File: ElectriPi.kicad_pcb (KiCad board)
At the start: 2 copper layers, 65 x 56 mm, 45 parts, among them J1 2444, J2 JST XH 01x02, J3 JST XH 01x02, J6 Raspberry_Pi_2_3, J8 JST XH 01x02, Q1 30V 4A 44mΩ, Q2 50nA 150V 200mW 200mA, Q3 30V 4A 44mΩ, U1 XL4015

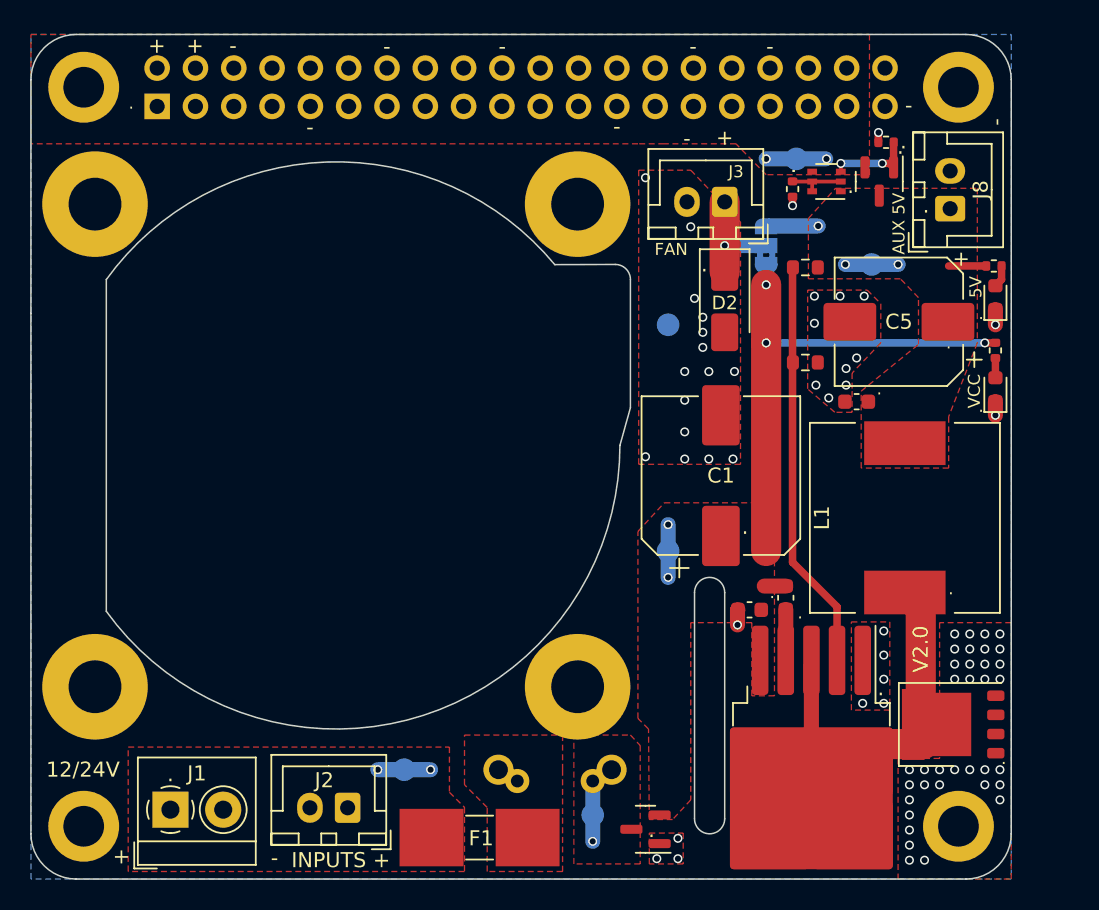
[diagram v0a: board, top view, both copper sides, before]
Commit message: First pass of layout complete
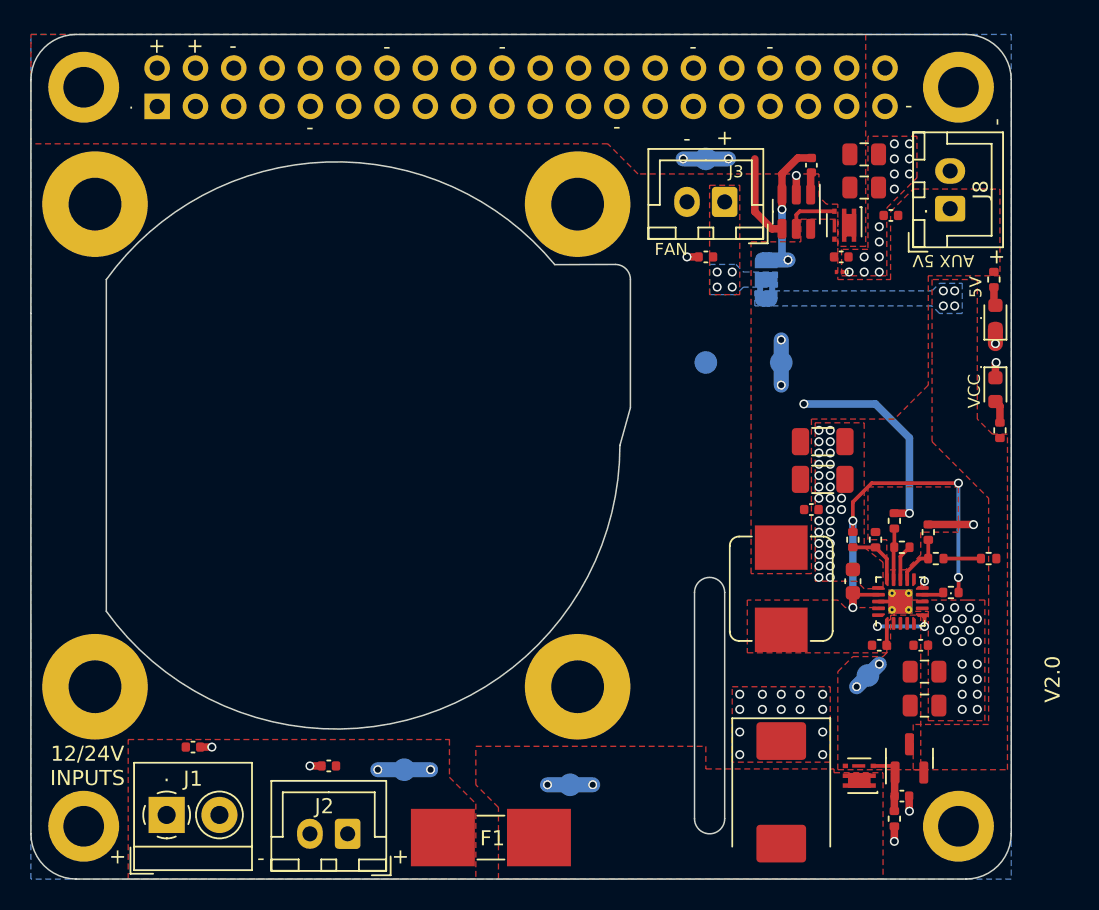
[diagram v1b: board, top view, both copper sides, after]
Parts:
- removed D2: SS54, Diode_SMD:D_SMA
- removed the G*** at (135.1, 81.0)
- removed Q3: 30V 4A 44mΩ, Package_TO_SOT_SMD:SOT-23
- removed R10: 10K, Resistor_SMD:R_0603_1608Metric
- removed R2: 47K, Resistor_SMD:R_0402_1005Metric
- removed R9: 3.3K, Resistor_SMD:R_0603_1608Metric
- removed TH1: ICL, Inrush_Limiter:5_OR_7pt5_PITCH_ICL
- added C10: 0.1uF, Capacitor_SMD:C_0402_1005Metric, F.Cu at (139.0, 68.0)
- added C11: 22 uF, Capacitor_SMD:C_0805_2012Metric, F.Cu at (140.5, 63.4)
- added C12: 0.1uF, Capacitor_SMD:C_0402_1005Metric, F.Cu at (96.0, 100.5)
- added C13: 0.1uF, Capacitor_SMD:C_0402_1005Metric, F.Cu at (105.0, 101.8)
- added C14: 0.1uF, Capacitor_SMD:C_0402_1005Metric, F.Cu at (130.0, 68.0)
- added C15: 0.1uF, Capacitor_SMD:C_0402_1005Metric, F.Cu at (142.3, 65.2)
- added C16: 22 uF, Capacitor_SMD:C_0805_2012Metric, F.Cu at (140.5, 61.2)
- added C17: 0.1uF, Capacitor_SMD:C_0402_1005Metric, F.Cu at (143.0, 103.8)
- added C6: 0.1uF, Capacitor_SMD:C_0402_1005Metric, F.Cu at (144.2, 93.8)
- added C7: 0.1uF, Capacitor_SMD:C_0402_1005Metric, F.Cu at (137.0, 84.8)
- added C8: 0.1uF, Capacitor_SMD:C_0402_1005Metric, F.Cu at (141.5, 93.8)
- added C9: 0.1uF, Capacitor_SMD:C_0402_1005Metric, F.Cu at (137.0, 61.9)
- added D4: BZX84-C13, Package_TO_SOT_SMD:SOT-23, F.Cu at (143.5, 101.2)
- added D6: PESD5V0C1BSFYL, Diode_SMD:Nexperia_DSN0603-2_0.6x0.3mm_P0.4mm, F.Cu at (138.8, 69.0)
- added IC2: TPS51397ARJER, Package_DFN_QFN:QFN-20-1EP_3x3mm_P0.45mm_EP1.6x1.6mm_ThermalVias, F.Cu at (142.9, 90.8)
- added R11: 33K, Resistor_SMD:R_0402_1005Metric, F.Cu at (144.8, 86.2)
- added R12: 110K, Resistor_SMD:R_0402_1005Metric, F.Cu at (146.2, 90.2)
- added R13: 110K, Resistor_SMD:R_0402_1005Metric, F.Cu at (142.5, 85.5)
- added R14: 15K, Resistor_SMD:R_0402_1005Metric, F.Cu at (143.0, 87.2)
- added R3: 110K, Resistor_SMD:R_0402_1005Metric, F.Cu at (142.5, 105.2)
- added R4: 180K, Resistor_SMD:R_0402_1005Metric, F.Cu at (139.8, 86.8)
- added R5: 33K, Resistor_SMD:R_0402_1005Metric, F.Cu at (141.2, 86.8)
- added R7: 110K, Resistor_SMD:R_0402_1005Metric, F.Cu at (145.2, 88.0)
- C1: value 220uF -> 22 uF; footprint Capacitor_SMD:CP_Elec_10x10 -> Capacitor_SMD:C_0805_2012Metric
- C2: value 1 uF -> 22 uF; footprint Capacitor_SMD:C_0603_1608Metric -> Capacitor_SMD:C_0805_2012Metric
- C4: value 1 uF -> 100uF; footprint Capacitor_SMD:C_0603_1608Metric -> Capacitor_SMD:C_1206_3216Metric
- C5: value 1000uF -> 100uF; footprint Capacitor_SMD:CP_Elec_8x10 -> Capacitor_SMD:C_1206_3216Metric
- D1: value V30K45 -> XMC7K24CA; footprint Package_DFN_QFN:PQFN-8-EP_6x5mm_P1.27mm_Generic -> Diode_SMD:D_SMC
- L1: value 47 uH -> 1.8 uH; footprint Inductor_SMD:L_12x12mm_H6mm -> Inductor_SMD:L_Bourns_SRP7028A_7.3x6.6mm
- Q1: value 30V 4A 44mΩ -> SiA471DJ; footprint Package_TO_SOT_SMD:SOT-23 -> Package_TO_SOT_SMD:Vishay_PowerPAK_SC70-6L_Single
- Q2: value 50nA 150V 200mW 200mA -> SiA430DJT; footprint Package_TO_SOT_SMD:SOT-363_SC-70-6 -> Package_TO_SOT_SMD:Vishay_PowerPAK_SC70-6L_Single
- R1: value 10K -> 33K
- R6: value 1kR -> 1K
- R8: value 10kR -> 10K
- U1: value XL4015 -> LM74700; footprint Package_TO_SOT_SMD:TO-263-5_TabPin3 -> Package_TO_SOT_SMD:SOT-23-6
- moved U1 37.4 mm to (136.0, 65.0)
- moved R1 27.7 mm to (148.8, 88.0), turned to 0 degrees
- moved C1 20.4 mm to (144.5, 97.8), turned to 0 degrees
- moved TP4 15.6 mm to (140.8, 95.8)
- moved Q1 14.6 mm to (140.2, 102.4)
- moved D1 12.3 mm to (135.0, 103.5), turned to -90 degrees
- moved C2 12.3 mm to (144.5, 95.5), turned to 0 degrees
- moved C5 11.6 mm to (137.8, 82.8), turned to 0 degrees
- moved G*** 9.78 mm to (133.8, 83.0)
- moved L1 9.45 mm to (135.0, 90.0)
- moved TP1 8.85 mm to (135.0, 75.0)
- moved TP5 6.00 mm to (130.0, 61.5)
- moved R8 5.31 mm to (149.5, 79.5), turned to -90 degrees
- moved C3 4.58 mm to (139.8, 89.5)
- moved TP6 3.54 mm to (130.0, 75.0)
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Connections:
- C1 pad 1: VCC -> Vin
- C2 pad 1: VCC -> Vin
- C3 pad 1: Net-(U1-VC) -> VCC
- C3 pad 2: VCC -> GND
- D1 pad 2: GND -> Net-(D1-A2)
- F1 pad 2: Net-(F1-Pad2) -> Net-(D1-A2)
- JP1 pad 1: VCC -> Vin
- L1 pad 1: Net-(U1-SW) -> SW
- Q1 pad 1: GND -> Net-(D1-A2)
- Q1 pad 3: Net-(Q1-D) -> Net-(D4-A)
- Q2 pad 1: +5V -> 5V_PI
- Q2 pad 3: Net-(Q2B-C2) -> Net-(Q2-G)
- Q2 pad 4: 5V_PI -> +5V
- R1 pad 1: Net-(Q2A-B1) -> Net-(R1-Pad1)
- R1 pad 2: GND -> Vin
- R8 pad 2: VCC -> Vin
- TP3 pad 1: Net-(Q1-D) -> Net-(D1-A2)
- TP4 pad 1: VCC -> Vin
- U1 pad 1: GND -> Net-(U1-VCAP)
- U1 pad 2: Net-(U1-FB) -> GND
- U1 pad 3: Net-(U1-SW) -> +5V
- U1 pad 4: Net-(U1-VC) -> 5V_PI
- U1 pad 5: VCC -> Net-(Q2-G)
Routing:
- net Net-(U1-FB): track 27.2 -> 0.00 mm
- net Net-(U1-SW): track 22.9 -> 0.00 mm
- net +5V: track 9.44 -> 26.6 mm, vias 3 -> 6
- net VCC: track 39.1 -> 25.2 mm, vias 5 -> 4
- net GND: track 4.18 -> 15.4 mm, vias 72 -> 87
- net Net-(J3-Pin_1): track 7.40 -> 0.00 mm, vias 1 -> 4
- net Net-(Q2B-C2): track 5.81 -> 0.00 mm, vias 2 -> 0
- net 5V_PI: track 3.95 -> 8.77 mm
- net Net-(D4-A): track 0.00 -> 4.46 mm
- net Net-(Q1-D): track 4.00 -> 0.00 mm, vias 1 -> 0
- net Net-(IC2-MODE): track 0.00 -> 3.95 mm
- net SW: track 0.00 -> 3.94 mm, vias 0 -> 2
- net Net-(Q2A-B1): track 3.84 -> 0.00 mm
- net Net-(Q2-G): track 0.00 -> 3.56 mm
- net Net-(IC2-EN): track 0.00 -> 3.52 mm
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- added copper zone on F.Cu, net Net-(D1-A2)
- added copper zone on B.Cu, net Net-(J3-Pin_1)
- added copper zone on F.Cu, net Net-(J3-Pin_1)
- added copper zone on F.Cu, net SW
- added copper zone on B.Cu, net Vin
- added copper zone on F.Cu, net Vin
- removed copper zone on F.Cu, net Net-(F1-Pad2)
- removed copper zone on F.Cu, net Net-(Q1-D)
- removed copper zone on F.Cu, net VCC
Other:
- board text added: "12/24V INPUTS"
- board text removed: "12/24V"
- board text removed: "INPUTS"
- board text removed: "Manufactured by LDO Motors"

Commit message: Added back JLC
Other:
- board text added: "JLCJLCJLCJLC"
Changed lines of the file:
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@@
     (effects (font (size 1.3 1.3) (thickness 0.2)) (justify mirror))
+  )
+  (gr_text "JLCJLCJLCJLC" (at 88 75 90) (layer "B.SilkS")
+    (effects (font (size 1 1) (thickness 0.15)) (justify left bottom mirror))
   )
   (gr_text "+" (at 131.25 66.5) (layer "B.SilkS")

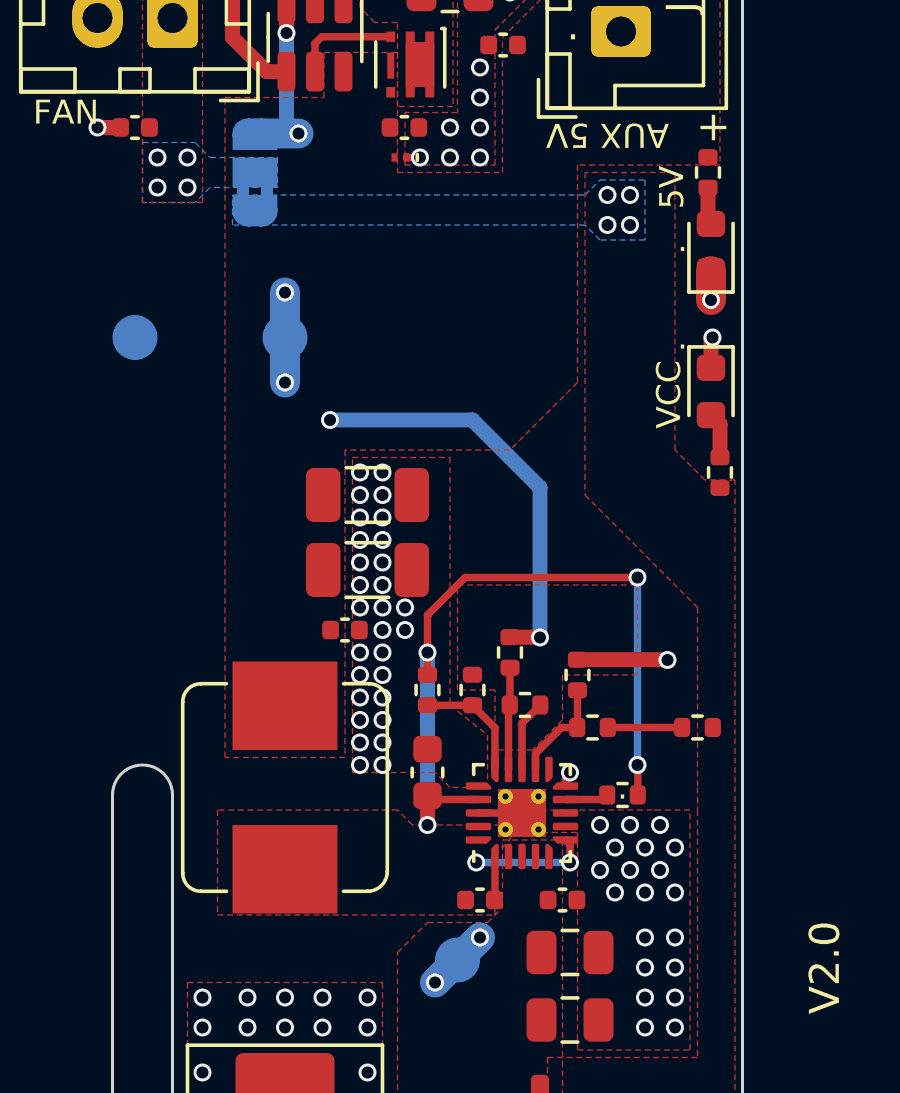
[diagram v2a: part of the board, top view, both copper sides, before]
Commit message: Some cleanup and updated logo to avoid ERC warnings
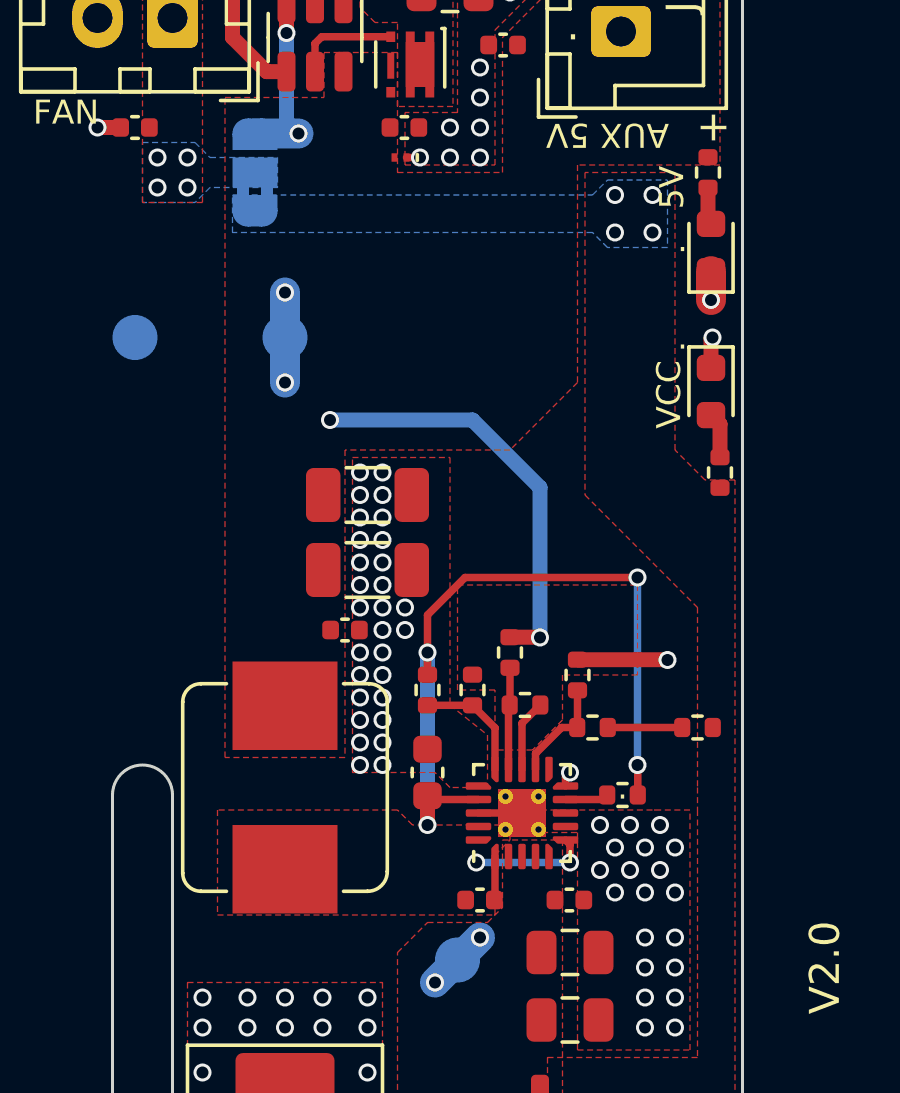
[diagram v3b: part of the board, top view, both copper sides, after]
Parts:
- moved C6 0.23 mm to (144.5, 93.8)
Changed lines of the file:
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@@
   )
   (footprint "Capacitor_SMD:C_0402_1005Metric" (layer "F.Cu")
-    (at 144.25 93.75)
+    (at 144.48 93.75)
     (descr "Capacitor SMD 0402 (1005 Metric), square (rectangular) end terminal, IPC_7351 nominal, (Body size source: IPC-SM-782 page 76, https://www.pcb-3d.com/wordpress/wp-content/uploads/ipc-sm-782a_amendment_1_and_2.pdf), generated with kicad-footprint-generator")
     (tags "capacitor")
@@
         (xy -2.5 2.656904)
         (xy -1.875 2.656904)
-        (xy -1.875 2.344327)
-        (xy -4.0625 2.344327)
-        (xy -4.0625 2.03175)
-        (xy -5.625 2.03175)
+        (xy -1.875 2.444327)
+        (xy -4.1625 2.444327)
+        (xy -4.1625 2.13175)
+        (xy -5.625 2.13175)
         (xy -5.625 2.344327)
         (xy -5.3125 2.344327)
@@
         (xy -1.25 0.468866)
         (xy -1.5625 0.468866)
-        (xy -1.5625 0.156289)
-        (xy -2.1875 0.156289)
-        (xy -2.1875 -0.156289)
-        (xy -3.4375 -0.156289)
-        (xy -3.4375 -0.468865)
-        (xy -5.625 -0.468865)
+        (xy -1.5625 0.256289)
+        (xy -2.2875 0.256289)
+        (xy -2.2875 -0.056289)
+        (xy -3.5375 -0.056289)
+        (xy -3.5375 -0.368865)
+        (xy -5.625 -0.368865)
         (xy -5.625 -0.156289)
         (xy -5.9375 -0.156289)
-        (xy -5.9375 0.156289)
-        (xy -3.75 0.156289)
-        (xy -3.75 0.468866)
-        (xy -2.5 0.468866)
-        (xy -2.5 0.781443)
-        (xy -2.1875 0.781443)
-        (xy -2.1875 1.09402)
-        (xy -1.25 1.09402)
+        (xy -5.9375 0.056289)
+        (xy -3.65 0.056289)
+        (xy -3.65 0.368866)
+        (xy -2.4 0.368866)
+        (xy -2.4 0.681443)
+        (xy -2.0875 0.681443)
+        (xy -2.0875 0.99402)
+        (xy -1.25 0.99402)
       )
       (stroke (width 0) (type solid)) (fill solid) (layer "B.SilkS"))
@@
   (segment (start 135.05 67.8) (end 135.05 64.85) (width 0.5) (layer "B.Cu") (net 3))
   (segment (start 143.5 80) (end 141.25 77.75) (width 0.5) (layer "B.Cu") (net 3))
-  (via (at 146.5 71.25) (size 0.6) (drill 0.4) (layers "F.Cu" "B.Cu") (free) (net 4))
+  (via (at 147.25 71.5) (size 0.6) (drill 0.4) (layers "F.Cu" "B.Cu") (free) (net 4))
   (via (at 141.5 95) (size 0.6) (drill 0.4) (layers "F.Cu" "B.Cu") (net 4))
-  (via (at 145.75 70.25) (size 0.6) (drill 0.4) (layers "F.Cu" "B.Cu") (free) (net 4))
+  (via (at 146 70.25) (size 0.6) (drill 0.4) (layers "F.Cu" "B.Cu") (free) (net 4))
   (via (at 140 96.5) (size 0.6) (drill 0.4) (layers "F.Cu" "B.Cu") (net 4))
-  (via (at 145.75 71.25) (size 0.6) (drill 0.4) (layers "F.Cu" "B.Cu") (free) (net 4))
-  (via (at 146.5 70.25) (size 0.6) (drill 0.4) (layers "F.Cu" "B.Cu") (free) (net 4))
+  (via (at 146 71.5) (size 0.6) (drill 0.4) (layers "F.Cu" "B.Cu") (free) (net 4))
+  (via (at 147.25 70.25) (size 0.6) (drill 0.4) (layers "F.Cu" "B.Cu") (free) (net 4))
   (segment (start 140.75 95.75) (end 140 96.5) (width 1) (layer "B.Cu") (net 4))
   (segment (start 140.75 95.75) (end 141.5 95) (width 1) (layer "B.Cu") (net 4))
@@
       (pts
         (xy 133.25 70.25)
-        (xy 145 70.25)
-        (xy 145.5 69.75)
-        (xy 147 69.75)
-        (xy 147 71.75)
-        (xy 145.5 71.75)
-        (xy 145 71.25)
-        (xy 133.25 71.25)
+        (xy 145.25 70.25)
+        (xy 145.75 69.75)
+        (xy 147.75 69.75)
+        (xy 147.75 72)
+        (xy 145.75 72)
+        (xy 145.25 71.5)
+        (xy 133.25 71.5)
       )
     )
@@
       7918337e-72a4-44c8-8c58-9a146340ad2a
       7da3258a-a651-4d91-b3f7-fc6593abede1
-      80ebaf06-4c8d-45ab-948a-4f346d5f35a0
       95b7dd29-f615-4870-bcc5-a4cd388827ad
-      b712aee4-53c2-438d-99c2-7a62c07134bd
-      d1be9255-f98c-4da1-9145-d857ac0df4dd
       e0aa7816-f12c-414c-b26b-86100383c989
       e21a06e8-83be-4f61-a1a4-b639c1d72d76
